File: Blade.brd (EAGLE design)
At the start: 160 x 101.6 mm, 132 parts, among them IC1 THN10-2411WIR, IC2 MCP6064-E/SL, IC3 MCP6064-E/SL, IC4 MCP6064-E/SL, IC5 MAX488CSA, IC6 MOCD207MSOIC-8, IC7 MOCD207MSOIC-8, IC8 MOCD207MSOIC-8, Q1 12MHz, U1 ADR366WAUJZ, U2 ADR366WAUJZ, U3 ADS1148QPWRQ1, U4 ADS1148QPWRQ1, U5 ADS1148QPWRQ1, U6 LT1528, U7 S70FL01GS, U8 S70FL01GS, U9 STM32F77XXXLQFP208, X1 D-SUB9-H5M09RA, X2 D-SUB15-H5M15RA, X3 USBPTH

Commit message: ads added
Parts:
- added C45, C46, C48, C49: 100n, rcl:C0805
- added C47, C50, C53: 1u, rcl:C0805
- added C54, C57: 10n, rcl:C0805
- added C55, C58: 10u, rcl:C0805
- added IC10, IC9: MCP6064-E/SL, linear:SO14
- added L4, L5: 1m, rcl:L5650M
- added RN13, RN14, RN15, RN16, RN17, RN18: ?, resistor-dil:EXBS8V
- added U10, U11, U12: ADS1148QPWRQ1, ads11xx:TSSOP28
- added X_IN_10, X_IN_11, X_IN_12, X_IN_13, X_IN_14, X_IN_15: (no value), adafruit:SMA_EDGELAUNCH
- RN1, RN4: value 56k -> ?
- RN2, RN5: value 5k6 -> ?
- RN3, RN6: value 330 -> ?
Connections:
- new net IN_DMS_10: IC9.13, RN15.1, X_IN_13.P
- new net IN_DMS_11: IC10.2, RN18.4, X_IN_14.P
- new net IN_DMS_12: IC10.6, RN18.3, X_IN_15.P
- new net IN_DMS_7: IC9.2, RN15.4, X_IN_10.P
- new net IN_DMS_8: IC9.6, RN15.3, X_IN_11.P
- new net IN_DMS_9: IC9.9, RN15.2, X_IN_12.P
- new net N$53: C47.1, U10.9
- new net N$54: C50.1, U11.9
- new net N$57: C53.1, U12.9
- new net N$58: IC9.3, RN13.5, RN14.4
- new net N$59: IC9.5, RN13.6, RN14.3
- new net N$60: IC9.10, RN13.7, RN14.2
- new net N$61: IC9.12, RN13.8, RN14.1
- new net N$62: C54.2, IC9.4, L4.2
- new net N$63: IC10.3, RN16.5, RN17.4
- new net N$64: IC10.5, RN16.6, RN17.3
- new net N$65: RN16.7, RN17.2
- new net N$66: RN16.8, RN17.1
- new net N$67: C57.2, IC10.4, L5.2
- new net OUT_DMS_10: IC9.14, RN15.8, U10.17
- new net OUT_DMS_11: IC10.1, RN18.5, U12.11
- new net OUT_DMS_12: IC10.7, RN18.6, U12.17
- new net OUT_DMS_7: IC9.1, RN15.5, U11.11
- new net OUT_DMS_8: IC9.7, RN15.6, U11.17
- new net OUT_DMS_9: IC9.8, RN15.7, U10.11
- new net SPI3_CS2: U11.24
- new net SPI4_CS2: U10.24
- new net SPI5_CS2: U12.24
- net 3V3: now also C45.1, C46.1, C48.1, C49.1, L4.1, L5.1, U10.1, U10.22, U11.1, U11.22, U12.1, U12.22
- net 3V3REF: now also C55.2, RN13.1, RN13.2, RN13.3, RN13.4
- net 3V3REF2: now also C58.2, RN16.1, RN16.2, RN16.3, RN16.4
- net ADC1_DRDY: now also U11.25
- net ADC1_RES: now also U11.4
- net ADC1_START: now also U11.23
- net ADC2_DRDY: now also U10.25
- net ADC2_RES: now also U10.4
- net ADC2_START: now also U10.23
- net ADC3_DRDY: now also U12.25
- net ADC3_RES: now also U12.4
- net ADC3_START: now also U12.23
- net GND: now also C45.2, C46.2, C47.2, C48.2, C49.2, C50.2, C53.2, C54.1, C55.1, C57.1, C58.1, IC10.11, IC9.11, RN14.5, RN14.6, RN14.7, RN14.8, RN17.5, RN17.6, RN17.7, RN17.8, U10.10, U10.2, U10.21, U10.3, U11.10, U11.2, U11.21, U11.3, U12.10, U12.2, U12.21, U12.3, X_IN_10.GND@1, X_IN_10.GND@2, X_IN_10.GND@3, X_IN_10.GND@4, X_IN_11.GND@1, X_IN_11.GND@2, X_IN_11.GND@3, X_IN_11.GND@4, X_IN_12.GND@1, X_IN_12.GND@2, X_IN_12.GND@3, X_IN_12.GND@4, X_IN_13.GND@1, X_IN_13.GND@2, X_IN_13.GND@3, X_IN_13.GND@4, X_IN_14.GND@1, X_IN_14.GND@2, X_IN_14.GND@3, X_IN_14.GND@4, X_IN_15.GND@1, X_IN_15.GND@2, X_IN_15.GND@3, X_IN_15.GND@4
- net SPI3_MISO: now also U11.26
- net SPI3_MOSI: now also U11.27
- net SPI3_SCK: now also U11.28
- net SPI4_MISO: now also U10.26
- net SPI4_MOSI: now also U10.27
- net SPI4_SCK: now also U10.28
- net SPI5_MISO: now also U12.26
- net SPI5_MOSI: now also U12.27
- net SPI5_SCK: now also U12.28
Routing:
- net GND: track 1194.8 -> 1347.8 mm
- net IN_DMS_7: track 0.00 -> 30.9 mm
- net IN_DMS_8: track 0.00 -> 26.0 mm
- net IN_DMS_12: track 0.00 -> 19.0 mm
- net 3V3: track 692.4 -> 709.4 mm
- net IN_DMS_11: track 0.00 -> 17.0 mm
- net IN_DMS_9: track 0.00 -> 15.3 mm
- net IN_DMS_10: track 0.00 -> 10.5 mm
- net N$62: track 0.00 -> 9.97 mm, vias 0 -> 1
- net N$54: track 0.00 -> 4.81 mm, vias 0 -> 1
- net N$53: track 0.00 -> 3.76 mm, vias 0 -> 1
- net N$67: track 0.00 -> 3.16 mm, vias 0 -> 1
- net N$57: track 0.00 -> 3.11 mm, vias 0 -> 1
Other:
- board size 160 x 101.6 mm -> 160 x 106.7 mm
- board text removed: "Hard: blade Rev. 1 Soft: runner Rev."

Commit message: Foo
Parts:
- moved C55 4.41 mm to (66.4, 83.1), turned to 90 degrees
- moved RN13 1.91 mm to (62.2, 83.8)
- moved IC9 1.27 mm to (60.3, 90.8)
- moved RN15 1.27 mm to (60.3, 90.8)
- moved RN14 0.64 mm to (62.2, 84.5)
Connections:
- removed net 3V3REF3: U9.41
- net 3V3REF2: now also U9.41
- net SPI3_CS2: now also U9.18
- net SPI4_CS2: now also U9.19
- net SPI5_CS2: now also U9.20
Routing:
- net SPI4_CS2: track 0.00 -> 66.1 mm, vias 0 -> 2
- net SPI3_CS2: track 0.00 -> 49.8 mm, vias 0 -> 2
- net SPI5_CS2: track 0.00 -> 46.9 mm, vias 0 -> 4
- net IN_DMS_8: track 26.0 -> 14.2 mm
- net N$62: track 9.97 -> 0.00 mm, vias 1 -> 0
- net IN_DMS_7: track 30.9 -> 23.2 mm
- net N$54: track 4.81 -> 0.19 mm, vias 1 -> 0
- net N$57: track 3.11 -> 0.18 mm, vias 1 -> 0
- net IN_DMS_9: track 15.3 -> 16.6 mm
- net IN_DMS_10: track 10.5 -> 11.8 mm
- net DAPI_RX: track 79.3 -> 78.8 mm

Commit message: rerouting
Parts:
- added C52: 10n, rcl:C0805
- added R22: 100k, rcl:R0805
- added R23: 1k, rcl:R0805
- added R24, R25: ?, rcl:R0805
- added U13: ADR366WAUJZ, ADR360:SOT23-5
- moved C41 18.6 mm to (94.6, 65.4), turned to 90 degrees
- moved C53 16.2 mm to (72.0, 68.3), turned to 0 degrees
- moved C44 14.4 mm to (109.5, 47.4), turned to 90 degrees
- moved C36 12.5 mm to (100.7, 50.4)
- moved U12 12.2 mm to (74.3, 67.9)
- moved IC1 12.1 mm to (111.1, 55.2)
- moved R11 11.2 mm to (125.1, 12.1), turned to 180 degrees
- moved C39 10.1 mm to (94.0, 49.3)
- moved C38 9.53 mm to (114.3, 62.2)
- moved U11 9.09 mm to (86.4, 72.4)
- moved C43 8.91 mm to (109.5, 52.6)
- moved U$1 8.89 mm to (114.9, 52.1)
- moved RN13 7.62 mm to (62.2, 76.2)
- moved R10 7.61 mm to (128.1, 43.8), turned to 270 degrees
- moved IC7 7.10 mm to (122.6, 26.0)
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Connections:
- new net 3V3REF3: R24.2, U13.4, U9.41
- new net ADC4_DRDY: U11.25, U9.32
- new net ADC4_RES: U11.4, U9.31
- new net ADC4_START: U11.23, U9.30
- new net ADC5_DRDY: U10.25, U9.44
- new net ADC5_RES: U10.4, U9.37
- new net ADC5_START: U10.23, U9.35
- new net ADC6_DRDY: U12.25, U9.45
- new net ADC6_RES: U12.4, U9.33
- new net ADC6_START: U12.23, U9.38
- new net N$68: R22.1, U13.5
- new net N$69: R22.2, R24.1, R25.2
- new net N$70: R23.2, R25.1
- net 3V3REF2: no longer U9.41
- net 5V: now also C52.2, U13.3
- net ADC1_DRDY: no longer U11.25
- net ADC1_RES: no longer U11.4
- net ADC1_START: no longer U11.23
- net ADC2_DRDY: no longer U10.25
- net ADC2_RES: no longer U10.4
- net ADC2_START: no longer U10.23
- net ADC3_DRDY: no longer U12.25
- net ADC3_RES: no longer U12.4
- net ADC3_START: no longer U12.23
- net GND: now also C52.1, R23.1, U13.2
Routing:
- net GND: track 1347.8 -> 610.5 mm, vias 141 -> 22
- net 3V3: track 709.4 -> 809.9 mm, vias 26 -> 37
- net OUT_DMS_8: track 0.00 -> 62.6 mm, vias 0 -> 3
- net 28VGND: track 197.3 -> 259.8 mm, vias 35 -> 4
- net SPI3_MISO: track 79.6 -> 132.1 mm
- net ADC5_RES: track 0.00 -> 51.4 mm, vias 0 -> 4
- net SPI3_SCK: track 78.3 -> 128.2 mm
- net SPI3_CS2: track 49.8 -> 0.00 mm, vias 2 -> 0
- net SPI5_CS2: track 46.9 -> 0.00 mm, vias 4 -> 0
- net ADC5_START: track 0.00 -> 46.7 mm, vias 0 -> 2
- net OUT_DMS_7: track 0.00 -> 42.9 mm, vias 0 -> 2
- net ADC5_DRDY: track 0.00 -> 38.4 mm, vias 0 -> 2
- net OUT_DMS_11: track 0.00 -> 36.8 mm, vias 0 -> 1
- net ADC4_START: track 0.00 -> 33.7 mm
- net ADC4_RES: track 0.00 -> 32.6 mm, vias 0 -> 2
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- added copper zone on layer 15, net 28VGND
- added copper zone on layer 2, net 28VGND
- added copper zone on layer 15, net GND
- added copper zone on layer 2, net GND
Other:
- board text added: "h = 10.5mm"
- board text removed: "h = 9.9mm"

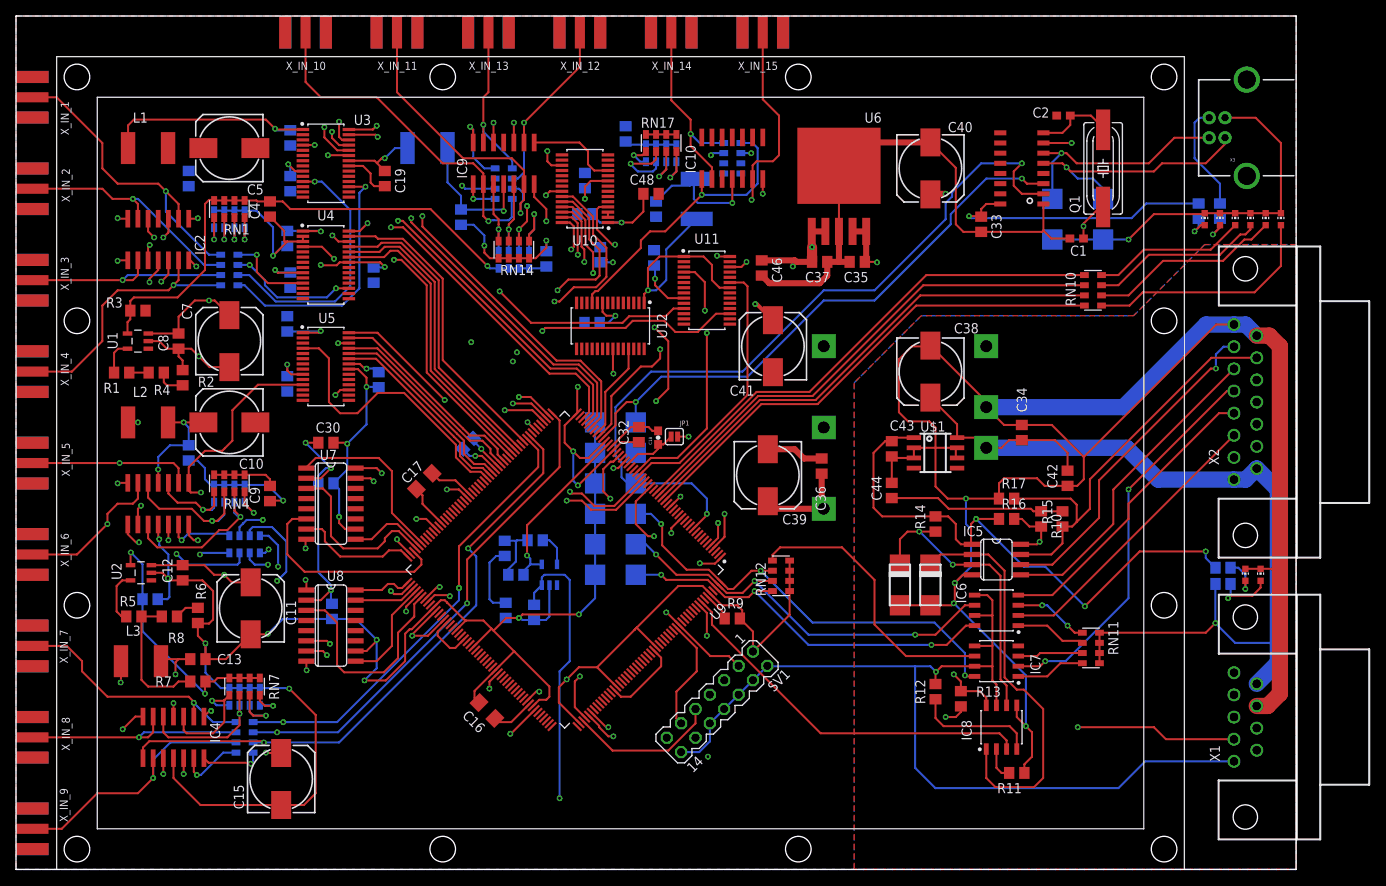
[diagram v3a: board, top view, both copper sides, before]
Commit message: bom added, text cleanup
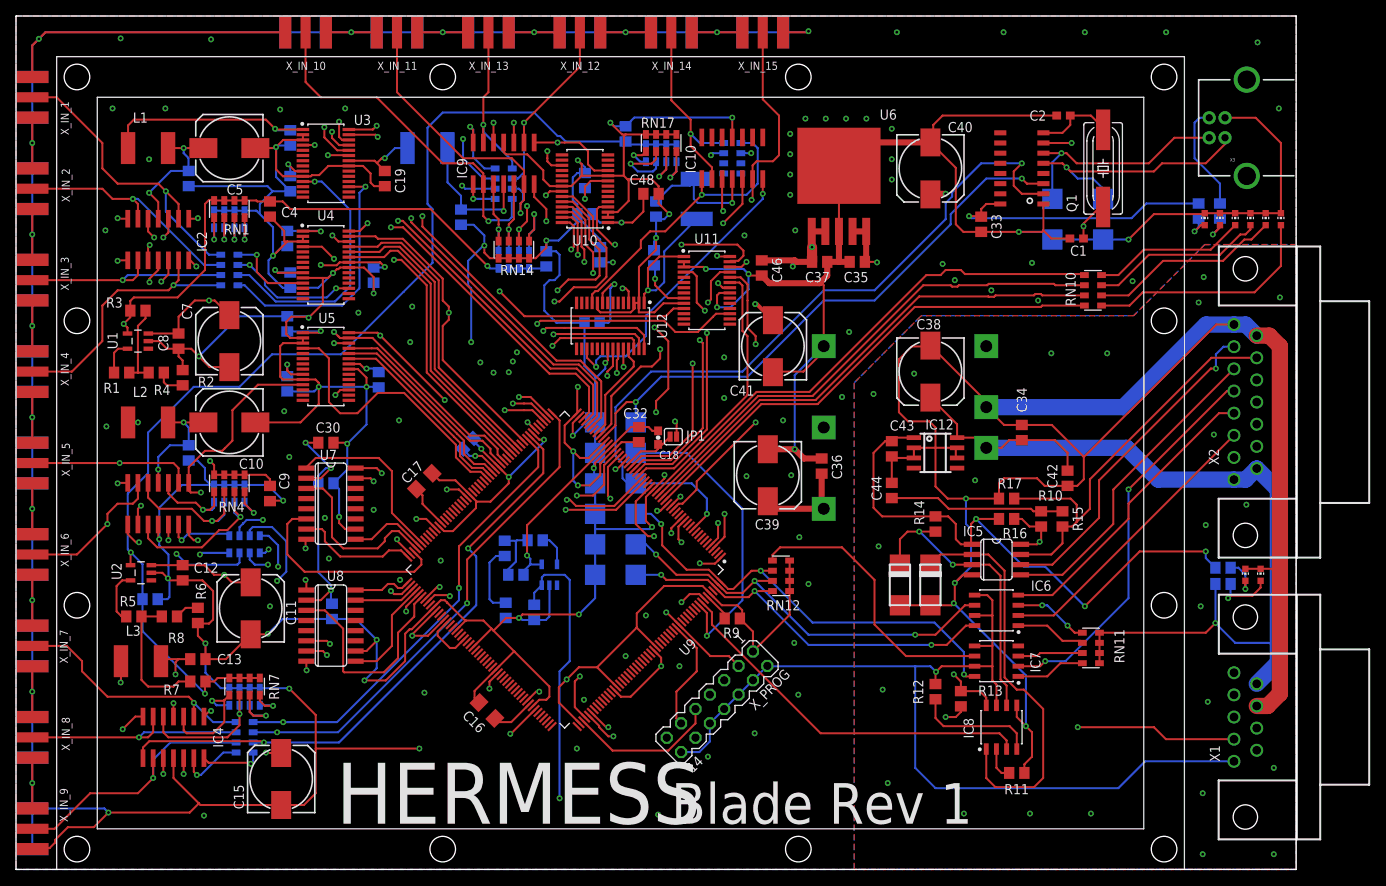
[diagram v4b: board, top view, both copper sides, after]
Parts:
- moved JP1 0.13 mm to (82.2, 54.1)
- renumbered SV1 to X_PROG, U$1 to IC12, U$2 to IC13
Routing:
- net GND: track 610.5 -> 1473.7 mm, vias 22 -> 131
- net 3V3REF2: track 38.1 -> 142.9 mm
- net SPI3_MOSI: track 38.4 -> 90.5 mm, vias 0 -> 2
- net ADC6_START: track 0.00 -> 45.9 mm, vias 0 -> 3
- net SPI5_MOSI: track 26.2 -> 70.1 mm, vias 0 -> 2
- net SPI5_SCK: track 55.0 -> 91.2 mm, vias 2 -> 4
- net SPI3_CS2: track 0.00 -> 35.6 mm, vias 0 -> 2
- net OUT_DMS_12: track 8.82 -> 43.7 mm, vias 2 -> 3
- net ADC6_RES: track 0.00 -> 34.3 mm, vias 0 -> 2
- net EXP_IN_OPT: track 49.0 -> 83.0 mm
- net ADC4_DRDY: track 0.00 -> 33.3 mm, vias 0 -> 2
- net 3V3REF: track 78.0 -> 106.3 mm, vias 1 -> 3
- net SPI5_CS2: track 0.00 -> 24.7 mm, vias 0 -> 2
- net SPI5_MISO: track 54.3 -> 78.2 mm, vias 2 -> 4
- net OUT_DMS_9: track 11.6 -> 31.1 mm, vias 0 -> 2
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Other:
- board text added: "Blade Rev 1"
- board text added: "HERMESS"

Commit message: finished routing Rev. 1
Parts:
- D5, D6: value ~5V2 -> 6V
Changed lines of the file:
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@@
 <layer number="49" name="Reference" color="7" fill="1" visible="yes" active="yes"/>
 <layer number="50" name="dxf" color="7" fill="1" visible="no" active="no"/>
-<layer number="51" name="tDocu" color="7" fill="1" visible="no" active="yes"/>
+<layer number="51" name="tDocu" color="7" fill="1" visible="yes" active="yes"/>
 <layer number="52" name="bDocu" color="7" fill="1" visible="yes" active="yes"/>
 <layer number="53" name="tGND_GNDA" color="7" fill="9" visible="no" active="no"/>
@@
 <wire x1="160.02" y1="106.68" x2="0" y2="106.68" width="0" layer="20"/>
 <wire x1="0" y1="106.68" x2="0" y2="0" width="0" layer="20"/>
-<dimension x1="-1.27" y1="0" x2="-1.27" y2="101.6" x3="-12.065" y3="50.8" textsize="1.778" layer="47"/>
-<dimension x1="0" y1="-1.27" x2="160.02" y2="-1.27" x3="80.01" y3="-5.08" textsize="1.778" layer="47"/>
 <polygon width="0.1524" layer="39">
 <vertex x="5.08" y="101.6"/>
@@
 </element>
 <element name="R9" library="rcl" library_urn="urn:adsk.eagle:library:334" package="R0805" package3d_urn="urn:adsk.eagle:package:23553/2" value="20k" x="89.535" y="31.369" smashed="yes">
-<attribute name="NAME" x="88.392" y="28.956" size="1.27" layer="25"/>
+<attribute name="NAME" x="91.821" y="30.607" size="1.27" layer="25"/>
 <attribute name="POPULARITY" value="86" x="89.535" y="31.369" size="1.778" layer="27" display="off"/>
 <attribute name="SPICEPREFIX" value="R" x="89.535" y="31.369" size="1.778" layer="27" display="off"/>
@@
 <attribute name="VALUE" x="125.603" y="44.45" size="1.27" layer="27" rot="R270"/>
 </element>
-<element name="D5" library="diodes" package="DMELF" value="~5V2" x="114.3" y="35.56" smashed="yes" rot="R90">
+<element name="D5" library="diodes" package="DMELF" value="6V" x="114.3" y="35.56" smashed="yes" rot="R90">
 <attribute name="NAME" x="113.03" y="29.845" size="1.27" layer="25" font="vector" ratio="16"/>
 <attribute name="NAME" x="113.03" y="29.845" size="1.27" layer="51" font="vector" ratio="16"/>
 <attribute name="VALUE" x="112.395" y="33.02" size="1.27" layer="27" font="vector" ratio="16" rot="R90"/>
 </element>
-<element name="D6" library="diodes" package="DMELF" value="~5V2" x="110.49" y="35.56" smashed="yes" rot="R90">
+<element name="D6" library="diodes" package="DMELF" value="6V" x="110.49" y="35.56" smashed="yes" rot="R90">
 <attribute name="NAME" x="109.22" y="29.845" size="1.27" layer="25" font="vector" ratio="16"/>
 <attribute name="NAME" x="109.22" y="29.845" size="1.27" layer="51" font="vector" ratio="16"/>
